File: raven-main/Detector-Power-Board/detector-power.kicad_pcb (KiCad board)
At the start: 2 copper layers, 37 x 44.5 mm, 36 parts, among them J1 DeployLipo, J2 Conn_01x06, J9 UCLipo, Q1 SQJQ100EL, T1 Transformer_1P_1S, U6 LM5185QPWPRQ1, U7 TPS7A4701xRGW, U8 TPS7A4701xRGW

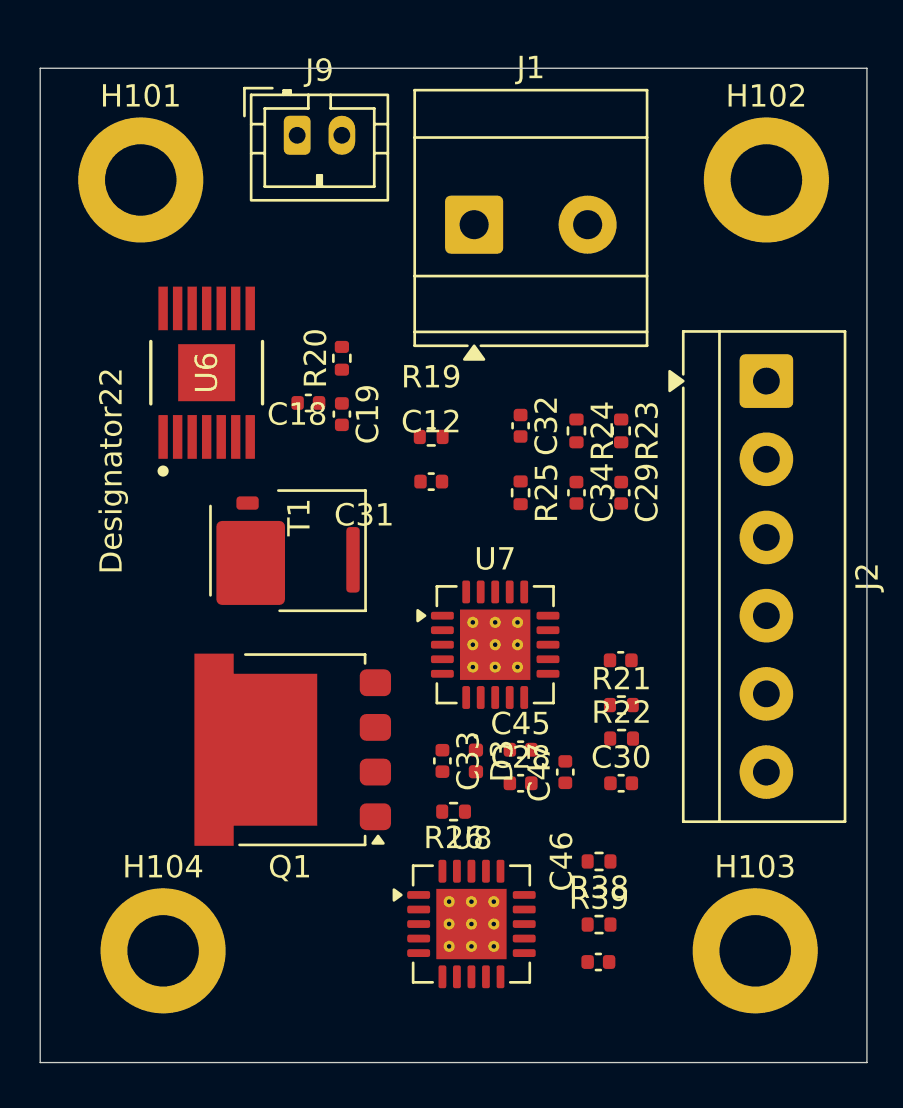
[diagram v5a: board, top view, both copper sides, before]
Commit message: Created pcb layout draft for power board
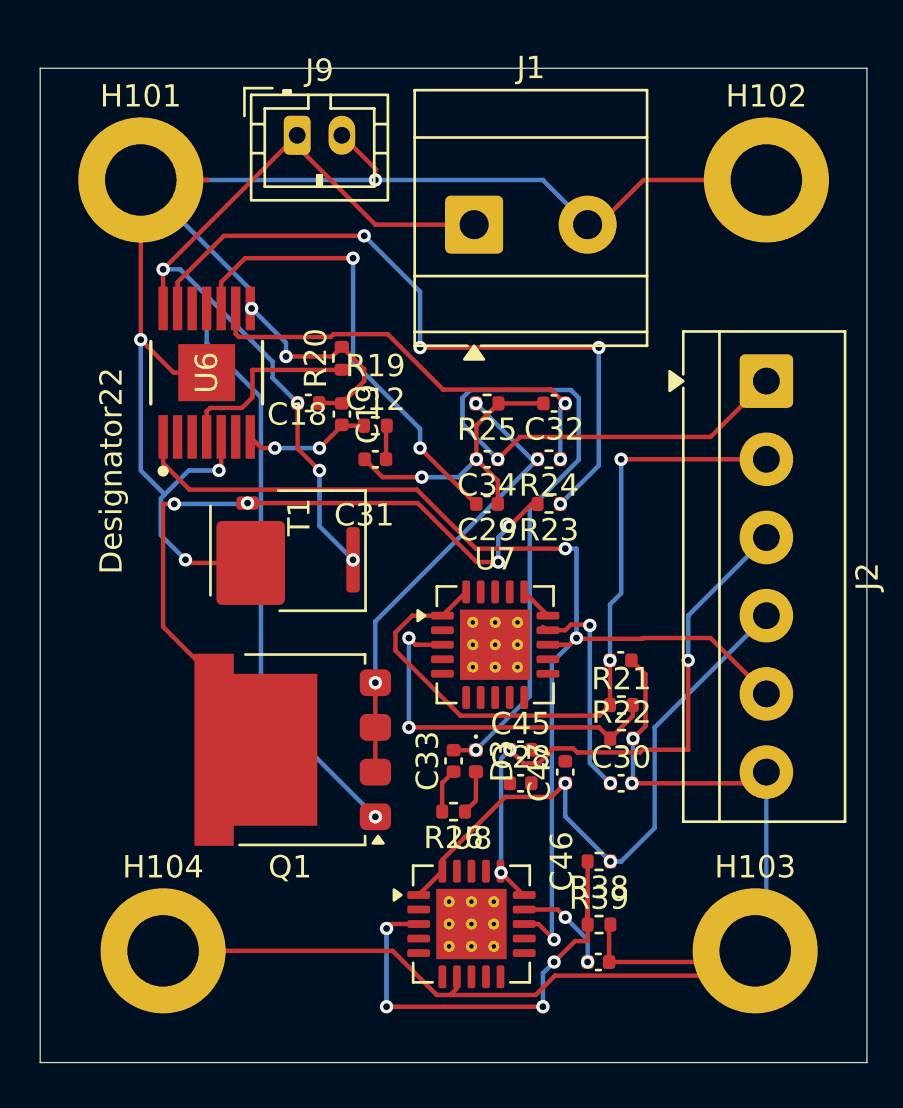
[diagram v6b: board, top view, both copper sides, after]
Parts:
- moved C29 6.02 mm to (130.5, 77.0), turned to 180 degrees
- moved R23 4.60 mm to (133.3, 77.0), turned to 180 degrees
- moved C34 4.27 mm to (130.5, 75.0), turned to 180 degrees
- moved R25 4.27 mm to (130.5, 72.5), turned to 180 degrees
- moved C12 2.69 mm to (125.5, 75.0)
- moved R19 2.55 mm to (125.5, 73.5)
- moved C32 1.80 mm to (133.5, 72.5), turned to 180 degrees
- moved R24 1.77 mm to (133.3, 75.0), turned to 180 degrees
- moved C33 0.50 mm to (129.0, 88.5), turned to 90 degrees
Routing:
- net GND: track 0.00 -> 155.6 mm, vias 0 -> 10
- net /ON-OFF: track 0.00 -> 51.8 mm, vias 0 -> 3
- net /Power_Out_50V: track 0.00 -> 41.0 mm, vias 0 -> 2
- net /BBIN: track 0.00 -> 38.6 mm, vias 0 -> 5
- net /Power_Out_5V: track 0.00 -> 33.4 mm, vias 0 -> 2
- net Net-(U6-FB): track 0.00 -> 32.1 mm, vias 0 -> 4
- net Net-(Q1-D): track 0.00 -> 28.1 mm, vias 0 -> 4
- net /Data_Out_3V3: track 0.00 -> 27.5 mm, vias 0 -> 2
- net /Data_In_5V: track 0.00 -> 26.8 mm, vias 0 -> 3
- net Net-(Q1-G): track 0.00 -> 25.9 mm, vias 0 -> 1
- net Net-(U8-SENSE/FB): track 0.00 -> 21.0 mm, vias 0 -> 4
- net Net-(U6-VCC): track 0.00 -> 20.8 mm, vias 0 -> 2
- net Net-(Q1-S-Pad2): track 0.00 -> 20.8 mm, vias 0 -> 3
- net Net-(U6-CS): track 0.00 -> 19.9 mm, vias 0 -> 2
- net Net-(U7-SENSE/FB): track 0.00 -> 16.8 mm, vias 0 -> 2
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
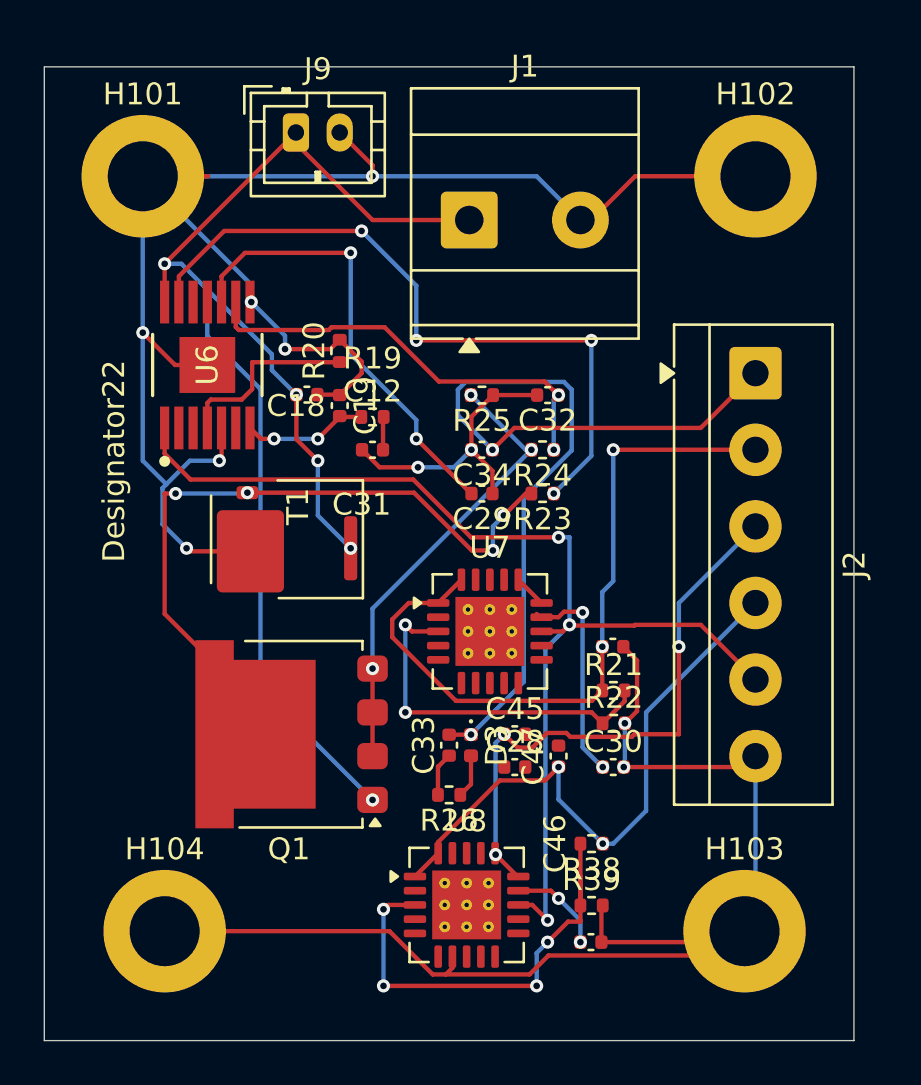
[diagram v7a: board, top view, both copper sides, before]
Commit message: Fixed silkscreen on power board
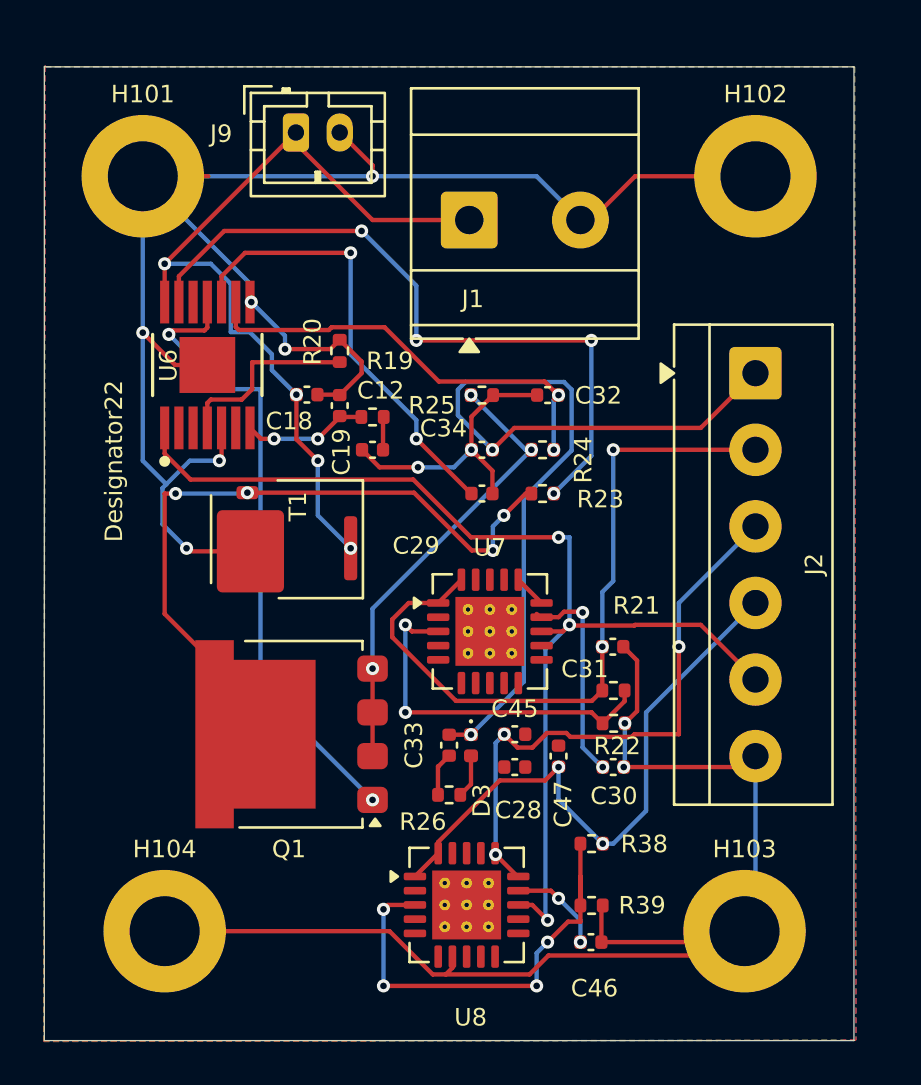
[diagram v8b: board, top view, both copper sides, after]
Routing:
- net Net-(Q1-G): track 25.9 -> 29.2 mm, vias 1 -> 2
- net /BBIN: track 38.6 -> 39.9 mm, vias 5 -> 4
- added copper zone on B.Cu, net GND
- added copper zone on F.Cu, net GND
